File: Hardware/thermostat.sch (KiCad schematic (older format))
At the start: 10 parts, among them K1 CONN_3_V, P1 CONN_01X01, P2 CONN_01X01

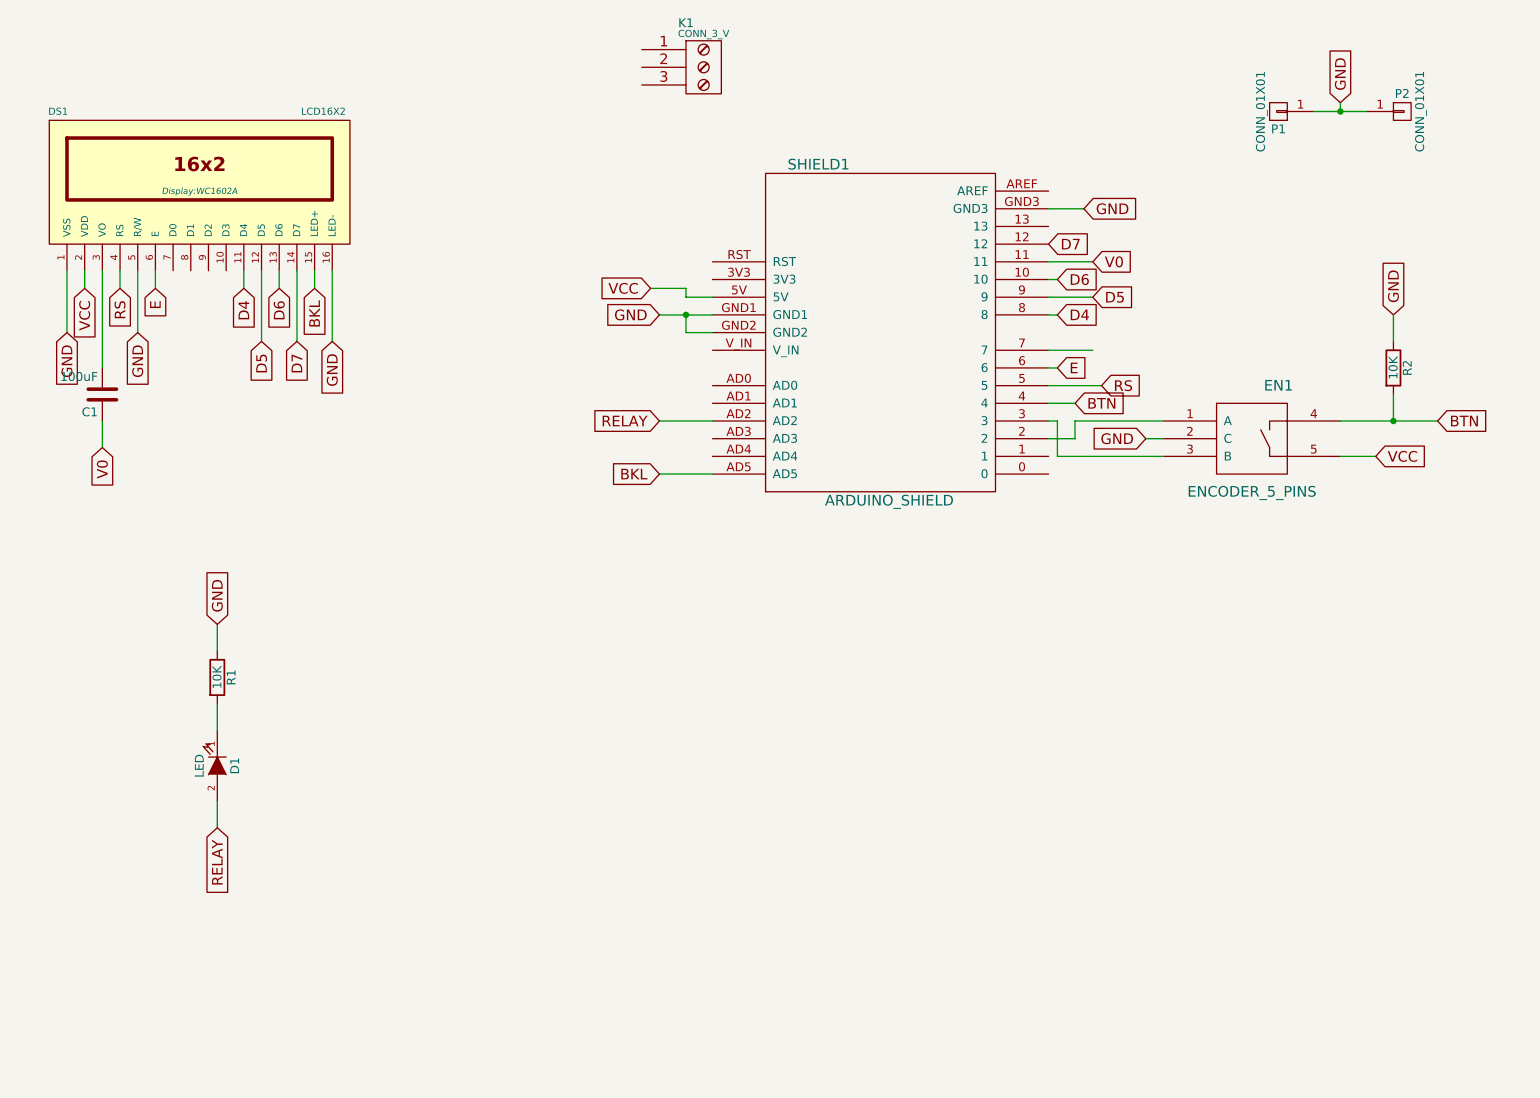
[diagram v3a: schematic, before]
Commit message: Added headers to improve ground connectivity and added relay and temp&hum headers
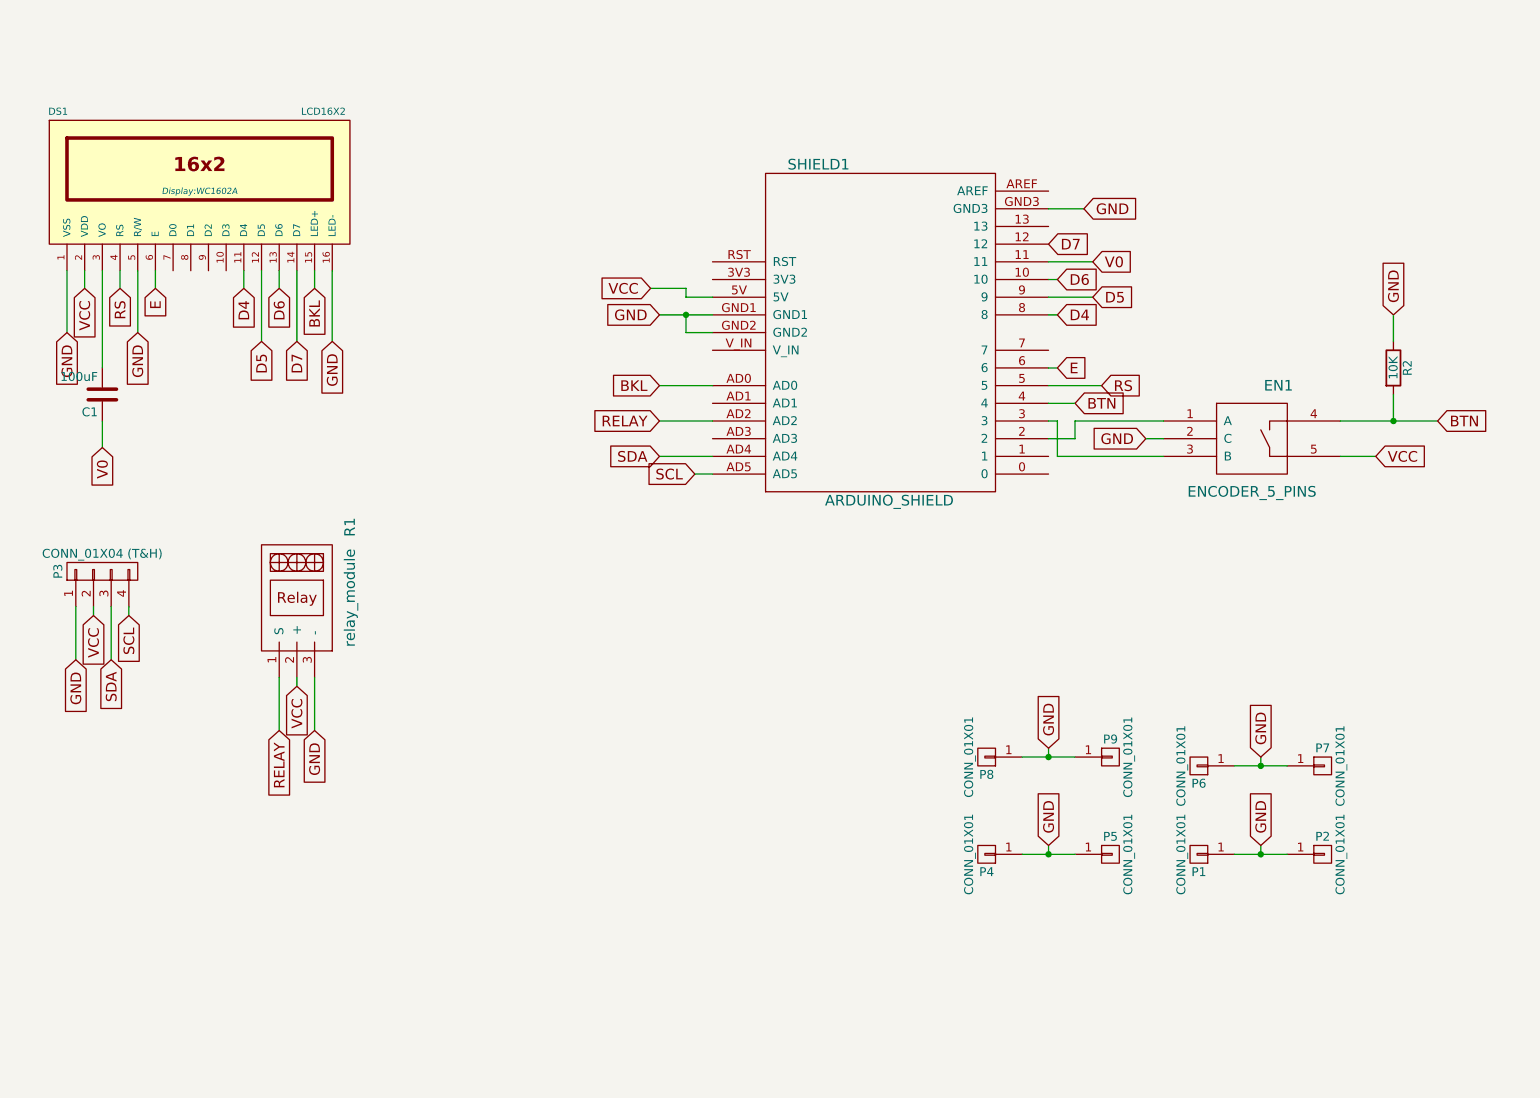
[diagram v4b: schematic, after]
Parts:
- removed D1: LED, LEDs:LED-3MM, symbol LED
- removed K1: CONN_3_V, borniers:bornier3_V, symbol CONN_3_V
- removed R1: 10K, Resistors_ThroughHole:Resistor_Horizontal_RM10mm, symbol R
- added P3: CONN_01X04 (T&H), Pin_Headers:Pin_Header_Straight_1x04, symbol CONN_01X04
- added P4, P5, P6, P7, P8, P9: CONN_01X01, library:header1x01, symbol CONN_01X01
- added R1: relay_module, Pin_Headers:Pin_Header_Angled_1x03, symbol relay_module
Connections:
- net BKL: now also SHIELD1.AD0; no longer SHIELD1.AD5
- net GND: now also P3.1 (P1), P4.1 (P1), P5.1 (P1), P6.1 (P1), P7.1 (P1), P8.1 (P1), P9.1 (P1), R1.3 (-)
- net RELAY: now also R1.1 (S)
- net VCC: now also P3.2 (P2), R1.2 (+)
- net SDA: now reaches SHIELD1.AD4
- net SDA: now also P3.3 (P3)
- new net SCL: P3.4 (P4), SHIELD1.AD5
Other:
- moved on the sheet: P1, P2
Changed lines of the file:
@@
 LIBS:encoder_5_pins
 LIBS:borniers
+LIBS:relay_module
 LIBS:thermostat-cache
 EELAYER 25 0
@@
 F 3 "" H 8150 3250 60  0000 C CNN
 	1    8150 3250
-	1    0    0    -1
-$EndComp
-$Comp
-L CONN_3_V K1
-U 1 1 55D36620
-P 5050 1150
-F 0 "K1" H 4950 1400 50  0000 C CNN
-F 1 "CONN_3_V" H 5050 1340 40  0000 C CNN
-F 2 "borniers:bornier3_V" H 5050 1150 60  0001 C CNN
-F 3 "" H 5050 1150 60  0000 C CNN
-	1    5050 1150
 	1    0    0    -1
 $EndComp
@@
 	7050 2550 7000 2550
 Wire Wire Line
-	7250 2750 7000 2750
-Wire Wire Line
 	7050 2850 7000 2850
 Wire Wire Line
@@
 Wire Wire Line
 	2850 2400 2850 2300
-Text GLabel 4800 3450 0    60   Input ~ 0
-BKL
-Wire Wire Line
-	4800 3450 5100 3450
+Text GLabel 5000 3450 0    60   Input ~ 0
+SCL
 Text GLabel 4800 2550 0    60   Input ~ 0
 GND
@@
 Wire Wire Line
 	8850 3350 8650 3350
-$Comp
-L R R1
-U 1 1 55D4AA7B
-P 2300 4600
-F 0 "R1" V 2380 4600 50  0000 C CNN
-F 1 "10K" V 2300 4600 50  0000 C CNN
-F 2 "Resistors_ThroughHole:Resistor_Horizontal_RM10mm" V 2230 4600 30  0001 C CNN
-F 3 "" H 2300 4600 30  0000 C CNN
-	1    2300 4600
-	1    0    0    -1
-$EndComp
-Text GLabel 2300 4300 1    60   Input ~ 0
-GND
-Wire Wire Line
-	2300 4450 2300 4300
-$Comp
-L LED D1
-U 1 1 55D4AB4B
-P 2300 5100
-F 0 "D1" H 2300 5200 50  0000 C CNN
-F 1 "LED" H 2300 5000 50  0000 C CNN
-F 2 "LEDs:LED-3MM" H 2300 5100 60  0001 C CNN
-F 3 "" H 2300 5100 60  0000 C CNN
-	1    2300 5100
-	0    1    1    0
-$EndComp
-Wire Wire Line
-	2300 4900 2300 4750
 Text GLabel 4800 3150 0    60   Input ~ 0
 RELAY
 Wire Wire Line
 	4800 3150 5100 3150
-Text GLabel 2300 5450 3    60   Input ~ 0
-RELAY
-Wire Wire Line
-	2300 5450 2300 5300
 Wire Wire Line
 	7000 3250 7150 3250
@@
 L CONN_01X01 P2
 U 1 1 55D4C211
-P 9000 1400
-F 0 "P2" H 9000 1500 50  0000 C CNN
-F 1 "CONN_01X01" V 9100 1400 50  0000 C CNN
-F 2 "library:header1x01" H 9000 1400 60  0001 C CNN
-F 3 "" H 9000 1400 60  0000 C CNN
-	1    9000 1400
+P 8550 5600
+F 0 "P2" H 8550 5700 50  0000 C CNN
+F 1 "CONN_01X01" V 8650 5600 50  0000 C CNN
+F 2 "library:header1x01" H 8550 5600 60  0001 C CNN
+F 3 "" H 8550 5600 60  0000 C CNN
+	1    8550 5600
 	1    0    0    -1
 $EndComp
@@
 L CONN_01X01 P1
 U 1 1 55D4C277
-P 8300 1400
-F 0 "P1" H 8300 1500 50  0000 C CNN
-F 1 "CONN_01X01" V 8400 1400 50  0000 C CNN
-F 2 "library:header1x01" H 8300 1400 60  0001 C CNN
-F 3 "" H 8300 1400 60  0000 C CNN
-	1    8300 1400
-	-1   0    0    1
-$EndComp
-Wire Wire Line
-	8500 1400 8800 1400
-Text GLabel 8650 1350 1    60   Input ~ 0
-GND
-Wire Wire Line
-	8650 1350 8650 1400
-Connection ~ 8650 1400
+P 7850 5600
+F 0 "P1" H 7850 5700 50  0000 C CNN
+F 1 "CONN_01X01" V 7950 5600 50  0000 C CNN
+F 2 "library:header1x01" H 7850 5600 60  0001 C CNN
+F 3 "" H 7850 5600 60  0000 C CNN
+	1    7850 5600
+	-1   0    0    1
+$EndComp
+Wire Wire Line
+	8050 5600 8350 5600
+Text GLabel 8200 5550 1    60   Input ~ 0
+GND
+Wire Wire Line
+	8200 5550 8200 5600
+Connection ~ 8200 5600
+$Comp
+L relay_module R1
+U 1 1 55DC4273
+P 2650 4400
+F 0 "R1" H 2000 4800 60  0000 C CNN
+F 1 "relay_module" H 2400 4800 60  0000 C CNN
+F 2 "Pin_Headers:Pin_Header_Angled_1x03" H 2650 4400 60  0001 C CNN
+F 3 "" H 2650 4400 60  0000 C CNN
+	1    2650 4400
+	0    1    1    0
+$EndComp
+Text GLabel 2650 4900 3    60   Input ~ 0
+RELAY
+Wire Wire Line
+	2650 4600 2650 4900
+Text GLabel 2850 4900 3    60   Input ~ 0
+GND
+Wire Wire Line
+	2850 4600 2850 4900
+Text GLabel 2750 4650 3    60   Input ~ 0
+VCC
+Wire Wire Line
+	2750 4650 2750 4600
+$Comp
+L CONN_01X04 P3
+U 1 1 55DC4D9E
+P 1650 4000
+F 0 "P3" H 1650 4250 50  0000 C CNN
+F 1 "CONN_01X04 (T&H)" V 1750 4000 50  0000 C CNN
+F 2 "Pin_Headers:Pin_Header_Straight_1x04" H 1650 4000 60  0001 C CNN
+F 3 "" H 1650 4000 60  0000 C CNN
+	1    1650 4000
+	0    -1   -1   0
+$EndComp
+Text GLabel 1500 4500 3    60   Input ~ 0
+GND
+Wire Wire Line
+	1500 4500 1500 4200
+Text GLabel 1600 4250 3    60   Input ~ 0
+VCC
+Wire Wire Line
+	1600 4250 1600 4200
+Wire Wire Line
+	1700 4200 1700 4500
+Wire Wire Line
+	1800 4200 1800 4250
+Text GLabel 4800 2950 0    60   Input ~ 0
+BKL
+Wire Wire Line
+	4800 2950 5100 2950
+Text GLabel 4800 3350 0    60   Input ~ 0
+SDA
+Wire Wire Line
+	4800 3350 5100 3350
+Text GLabel 1700 4500 3    60   Input ~ 0
+SDA
+Text GLabel 1800 4250 3    60   Input ~ 0
+SCL
+Wire Wire Line
+	5000 3450 5100 3450
+$Comp
+L CONN_01X01 P7
+U 1 1 55DC4A64
+P 8550 5100
+F 0 "P7" H 8550 5200 50  0000 C CNN
+F 1 "CONN_01X01" V 8650 5100 50  0000 C CNN
+F 2 "library:header1x01" H 8550 5100 60  0001 C CNN
+F 3 "" H 8550 5100 60  0000 C CNN
+	1    8550 5100
+	1    0    0    -1
+$EndComp
+$Comp
+L CONN_01X01 P6
+U 1 1 55DC4A6A
+P 7850 5100
+F 0 "P6" H 7850 5200 50  0000 C CNN
+F 1 "CONN_01X01" V 7950 5100 50  0000 C CNN
+F 2 "library:header1x01" H 7850 5100 60  0001 C CNN
+F 3 "" H 7850 5100 60  0000 C CNN
+	1    7850 5100
+	-1   0    0    1
+$EndComp
+Wire Wire Line
+	8050 5100 8350 5100
+Text GLabel 8200 5050 1    60   Input ~ 0
+GND
+Wire Wire Line
+	8200 5050 8200 5100
+Connection ~ 8200 5100
+$Comp
+L CONN_01X01 P5
+U 1 1 55DC4C11
+P 7350 5600
+F 0 "P5" H 7350 5700 50  0000 C CNN
+F 1 "CONN_01X01" V 7450 5600 50  0000 C CNN
+F 2 "library:header1x01" H 7350 5600 60  0001 C CNN
+F 3 "" H 7350 5600 60  0000 C CNN
+	1    7350 5600
+	1    0    0    -1
+$EndComp
+$Comp
+L CONN_01X01 P4
+U 1 1 55DC4C17
+P 6650 5600
+F 0 "P4" H 6650 5700 50  0000 C CNN
+F 1 "CONN_01X01" V 6750 5600 50  0000 C CNN
+F 2 "library:header1x01" H 6650 5600 60  0001 C CNN
+F 3 "" H 6650 5600 60  0000 C CNN
+	1    6650 5600
+	-1   0    0    1
+$EndComp
+Wire Wire Line
+	6850 5600 7150 5600
+Text GLabel 7000 5550 1    60   Input ~ 0
+GND
+Wire Wire Line
+	7000 5550 7000 5600
+Connection ~ 7000 5600
+$Comp
+L CONN_01X01 P9
+U 1 1 55DC52CE
+P 7350 5050
+F 0 "P9" H 7350 5150 50  0000 C CNN
+F 1 "CONN_01X01" V 7450 5050 50  0000 C CNN
+F 2 "library:header1x01" H 7350 5050 60  0001 C CNN
+F 3 "" H 7350 5050 60  0000 C CNN
+	1    7350 5050
+	1    0    0    -1
+$EndComp
+$Comp
+L CONN_01X01 P8
+U 1 1 55DC52D4
+P 6650 5050
+F 0 "P8" H 6650 5150 50  0000 C CNN
+F 1 "CONN_01X01" V 6750 5050 50  0000 C CNN
+F 2 "library:header1x01" H 6650 5050 60  0001 C CNN
+F 3 "" H 6650 5050 60  0000 C CNN
+	1    6650 5050
+	-1   0    0    1
+$EndComp
+Wire Wire Line
+	6850 5050 7150 5050
+Text GLabel 7000 5000 1    60   Input ~ 0
+GND
+Wire Wire Line
+	7000 5000 7000 5050
+Connection ~ 7000 5050
 $EndSCHEMATC

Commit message: Added 3 pin header for analog device, decrease pcb size
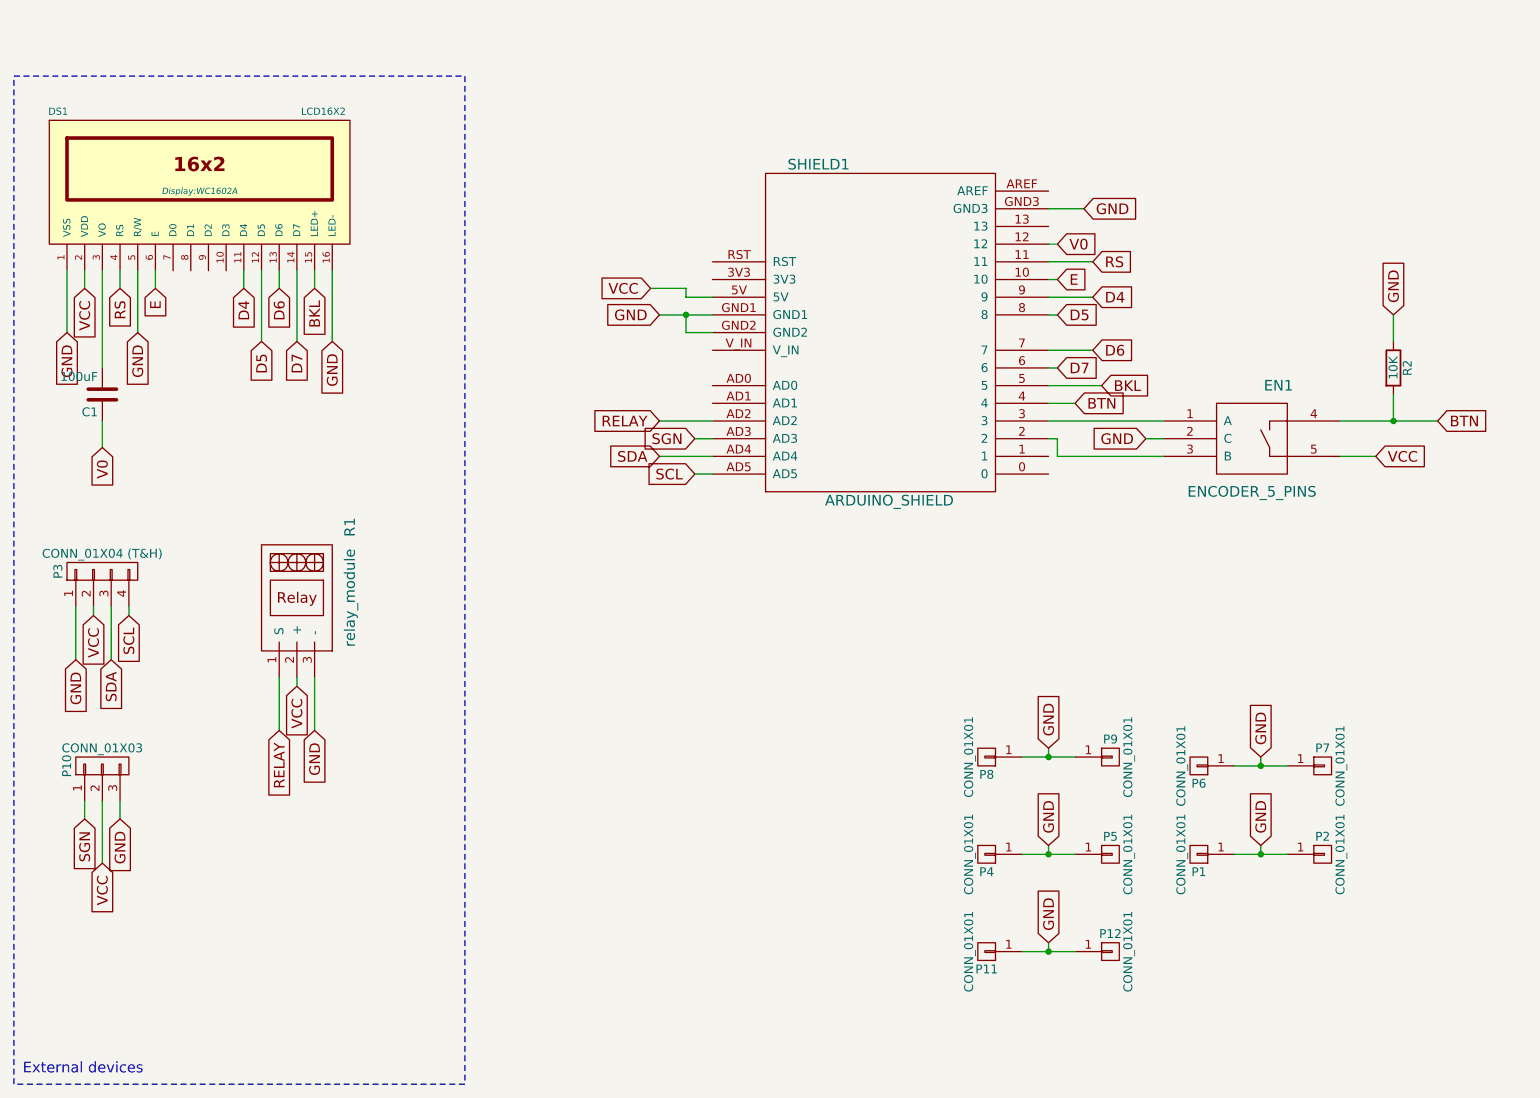
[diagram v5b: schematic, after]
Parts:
- added P10: CONN_01X03, Pin_Headers:Pin_Header_Angled_1x03, symbol CONN_01X03
- added P11, P12: CONN_01X01, library:header1x01, symbol CONN_01X01
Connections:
- net BKL: now also SHIELD1.5; no longer SHIELD1.AD0
- net D4: now also SHIELD1.9; no longer SHIELD1.8
- net D5: now also SHIELD1.8; no longer SHIELD1.9
- net D6: now also SHIELD1.7; no longer SHIELD1.10
- net D7: now also SHIELD1.6; no longer SHIELD1.12
- net E: now also SHIELD1.10; no longer SHIELD1.6
- net GND: now also P10.3 (P3), P11.1 (P1), P12.1 (P1)
- net RS: now also SHIELD1.11; no longer SHIELD1.5
- net V0: now also SHIELD1.12; no longer SHIELD1.11
- net VCC: now also P10.2 (P2)
- net at SHIELD1.2: now also EN1.3 (B); no longer EN1.1 (A)
- net at SHIELD1.3: now also EN1.1 (A); no longer EN1.3 (B)
- net SGN: now reaches SHIELD1.AD3
- net SGN: now also P10.1 (P1)
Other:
- note added: "External devices"
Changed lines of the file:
@@
 Text GLabel 1650 3300 3    60   Input ~ 0
 V0
-Text GLabel 7250 2250 2    60   Input ~ 0
+Text GLabel 7050 2150 2    60   Input ~ 0
 V0
 Text GLabel 1450 2650 3    60   Input ~ 0
@@
 Text GLabel 1750 2400 3    60   Input ~ 0
 RS
-Text GLabel 7300 2950 2    60   Input ~ 0
+Text GLabel 7250 2250 2    60   Input ~ 0
 RS
 Text GLabel 1850 2650 3    60   Input ~ 0
@@
 Text GLabel 2450 2400 3    60   Input ~ 0
 D4
-Text GLabel 7050 2550 2    60   Input ~ 0
+Text GLabel 7250 2450 2    60   Input ~ 0
 D4
 Text GLabel 2550 2700 3    60   Input ~ 0
@@
 Text GLabel 2750 2700 3    60   Input ~ 0
 D7
-Text GLabel 7250 2450 2    60   Input ~ 0
+Text GLabel 7050 2550 2    60   Input ~ 0
 D5
-Text GLabel 7050 2350 2    60   Input ~ 0
+Text GLabel 7250 2750 2    60   Input ~ 0
 D6
 Text GLabel 2950 2700 3    60   Input ~ 0
@@
 	4800 3150 5100 3150
 Wire Wire Line
-	7000 3250 7150 3250
-Wire Wire Line
-	7150 3250 7150 3150
-Wire Wire Line
-	7150 3150 7650 3150
-Wire Wire Line
-	7050 3350 7050 3150
-Wire Wire Line
-	7050 3150 7000 3150
-Text GLabel 7000 2150 2    60   Input ~ 0
+	7000 3150 7650 3150
+Text GLabel 7050 2850 2    60   Input ~ 0
 D7
 Wire Wire Line
 	7300 2950 7000 2950
-Text GLabel 7050 2850 2    60   Input ~ 0
+Text GLabel 7050 2350 2    60   Input ~ 0
 E
 $Comp
@@
 Wire Wire Line
 	1800 4200 1800 4250
-Text GLabel 4800 2950 0    60   Input ~ 0
+Text GLabel 7300 2950 2    60   Input ~ 0
 BKL
-Wire Wire Line
-	4800 2950 5100 2950
 Text GLabel 4800 3350 0    60   Input ~ 0
 SDA
@@
 	7000 5000 7000 5050
 Connection ~ 7000 5050
+Wire Wire Line
+	7050 2150 7000 2150
+Wire Wire Line
+	7250 2750 7000 2750
+Wire Wire Line
+	7000 3250 7050 3250
+Wire Wire Line
+	7050 3250 7050 3350
+Wire Notes Line
+	1150 1200 3700 1200
+Wire Notes Line
+	3700 1200 3700 6900
+Wire Notes Line
+	3700 6900 1150 6900
+Wire Notes Line
+	1150 6900 1150 1200
+Text Notes 1200 6850 0    60   ~ 0
+External devices
+$Comp
+L CONN_01X03 P10
+U 1 1 55DCA32B
+P 1650 5100
+F 0 "P10" H 1650 5300 50  0000 C CNN
+F 1 "CONN_01X03" V 1750 5100 50  0000 C CNN
+F 2 "Pin_Headers:Pin_Header_Angled_1x03" H 1650 5100 60  0001 C CNN
+F 3 "" H 1650 5100 60  0000 C CNN
+	1    1650 5100
+	0    -1   -1   0
+$EndComp
+Text GLabel 1750 5400 3    60   Input ~ 0
+GND
+Wire Wire Line
+	1750 5400 1750 5300
+Text GLabel 1650 5650 3    60   Input ~ 0
+VCC
+Wire Wire Line
+	1650 5650 1650 5300
+Text GLabel 1550 5400 3    60   Input ~ 0
+SGN
+Wire Wire Line
+	1550 5400 1550 5300
+Text GLabel 5000 3250 0    60   Input ~ 0
+SGN
+Wire Wire Line
+	5000 3250 5100 3250
+$Comp
+L CONN_01X01 P12
+U 1 1 55DCB058
+P 7350 6150
+F 0 "P12" H 7350 6250 50  0000 C CNN
+F 1 "CONN_01X01" V 7450 6150 50  0000 C CNN
+F 2 "library:header1x01" H 7350 6150 60  0001 C CNN
+F 3 "" H 7350 6150 60  0000 C CNN
+	1    7350 6150
+	1    0    0    -1
+$EndComp
+$Comp
+L CONN_01X01 P11
+U 1 1 55DCB05E
+P 6650 6150
+F 0 "P11" H 6650 6250 50  0000 C CNN
+F 1 "CONN_01X01" V 6750 6150 50  0000 C CNN
+F 2 "library:header1x01" H 6650 6150 60  0001 C CNN
+F 3 "" H 6650 6150 60  0000 C CNN
+	1    6650 6150
+	-1   0    0    1
+$EndComp
+Wire Wire Line
+	6850 6150 7150 6150
+Text GLabel 7000 6100 1    60   Input ~ 0
+GND
+Wire Wire Line
+	7000 6100 7000 6150
+Connection ~ 7000 6150
 $EndSCHEMATC

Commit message: improved pads
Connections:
- net GND: now also P10.1 (P1); no longer P10.3 (P3)
- net SGN: now also P10.3 (P3); no longer P10.1 (P1)
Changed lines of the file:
@@
 	0    -1   -1   0
 $EndComp
-Text GLabel 1750 5400 3    60   Input ~ 0
+Text GLabel 1550 5400 3    60   Input ~ 0
 GND
 Wire Wire Line
@@
 Wire Wire Line
 	1650 5650 1650 5300
-Text GLabel 1550 5400 3    60   Input ~ 0
+Text GLabel 1750 5400 3    60   Input ~ 0
 SGN
 Wire Wire Line
